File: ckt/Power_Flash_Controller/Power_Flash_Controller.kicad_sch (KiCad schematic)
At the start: 28 parts, among them J2 Screw_Terminal_01x03, J3 Screw_Terminal_01x03, J4 Screw_Terminal_01x03, K4 SANYOU_SRD_Form_C, K5 SANYOU_SRD_Form_C, K6 SANYOU_SRD_Form_C, Q1 BC857, Q2 BC857, Q3 BC857, U1 PC817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

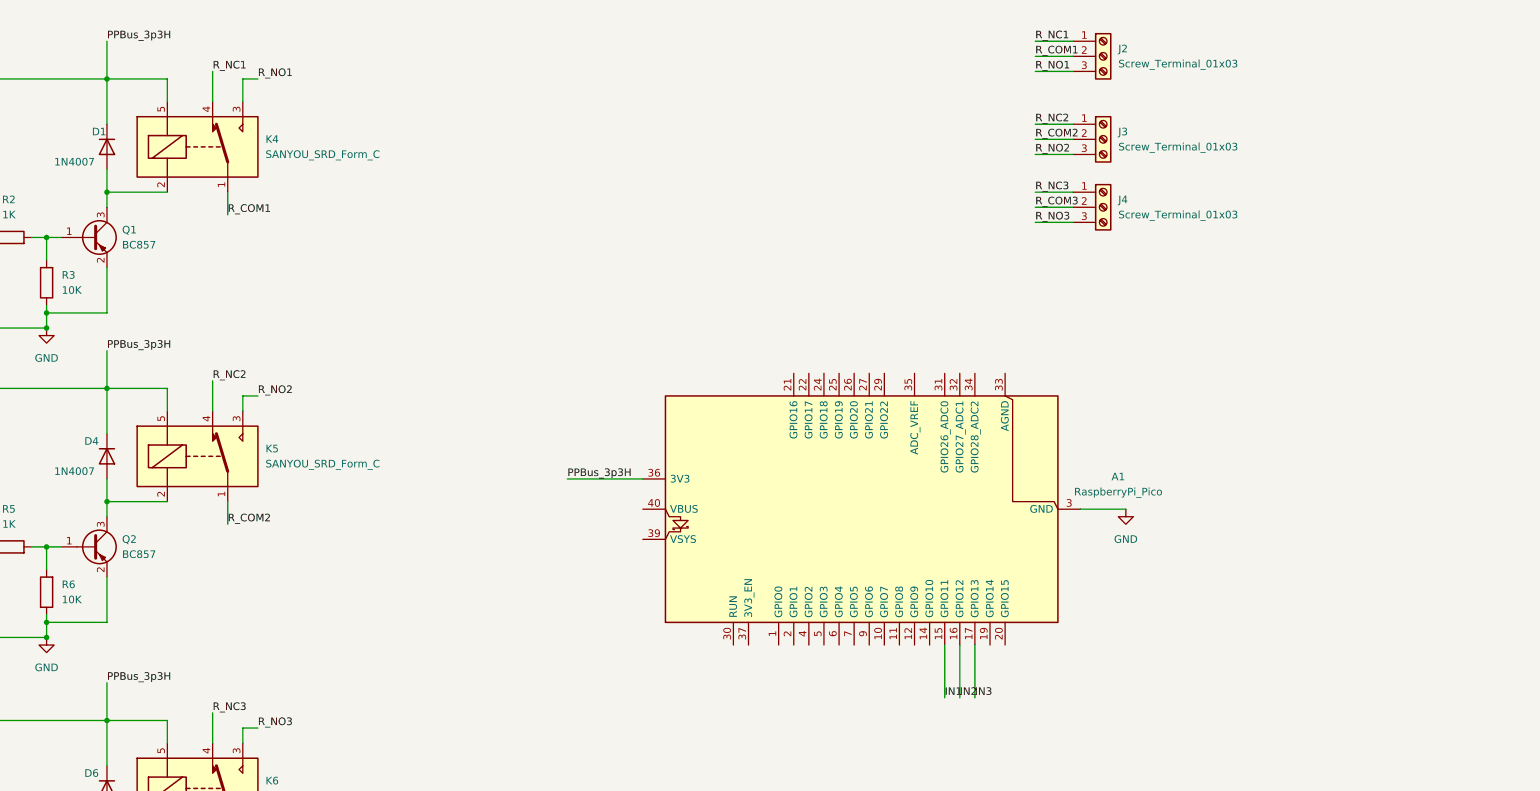
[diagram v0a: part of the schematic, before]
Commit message: Added connections for Ammeter and Voltmeter
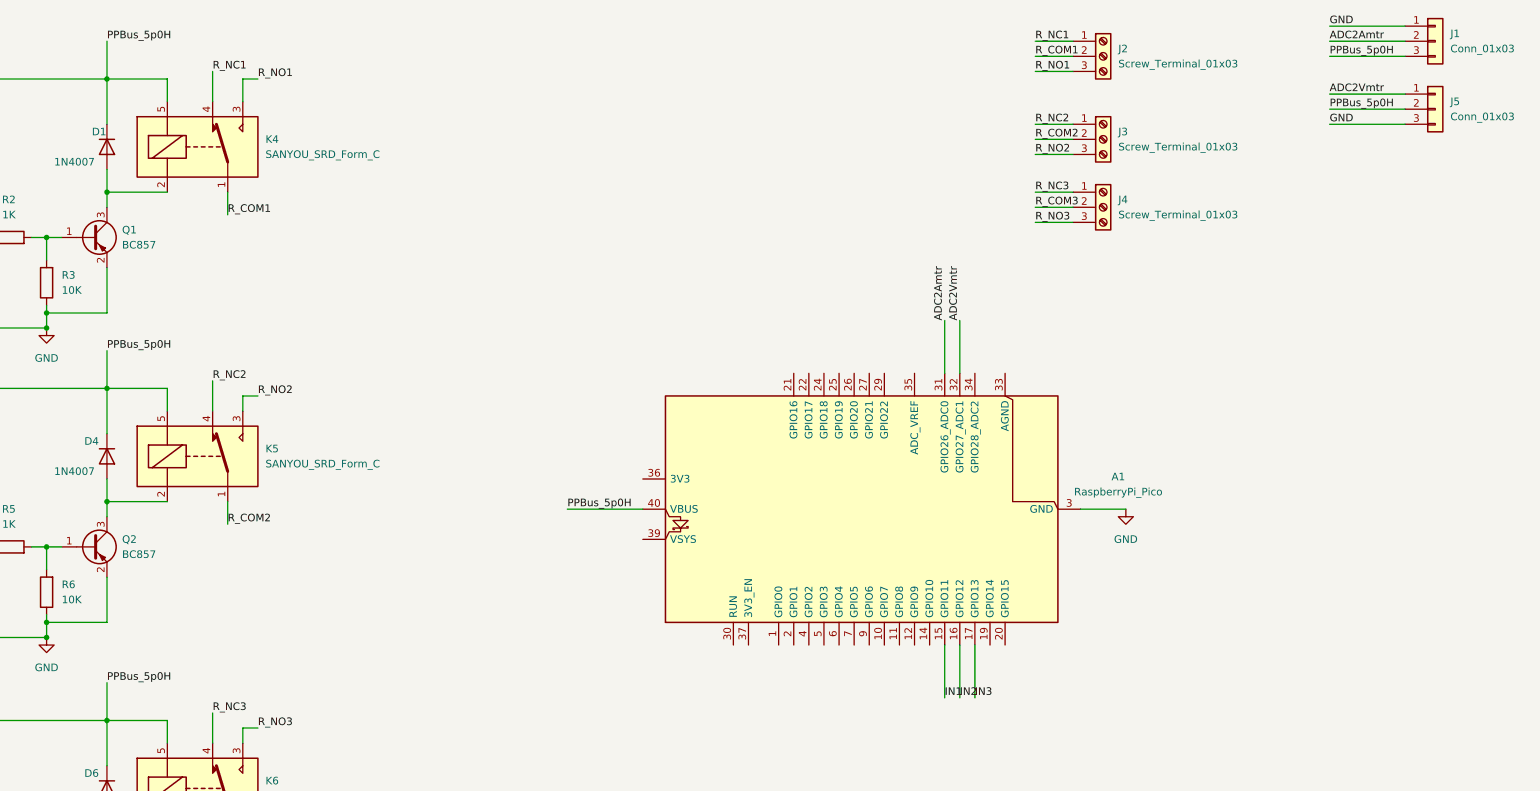
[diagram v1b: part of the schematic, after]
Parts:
- added J1, J5: Conn_01x03, Connector_PinHeader_2.54mm:PinHeader_1x03_P2.54mm_Vertical, symbol Connector_Generic:Conn_01x03
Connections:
- net GND: now also J1.1 (Pin_1), J5.3 (Pin_3)
- net ADC2Amtr: now reaches A1.31 (GPIO26_ADC0)
- net ADC2Amtr: now also J1.2 (Pin_2)
- net ADC2Vmtr: now reaches A1.32 (GPIO27_ADC1)
- net ADC2Vmtr: now also J5.1 (Pin_1)
- net PPBus_5p0H: now reaches A1.40 (VBUS)
- net PPBus_5p0H: now also D1.1 (K), D4.1 (K), D6.1 (K), K4.5, K5.5, K6.5, U1.4, U2.4, U3.4, J1.3 (Pin_3), J5.2 (Pin_2)
- removed net PPBus_3p3H: A1.36 (3V3), D1.1 (K), D4.1 (K), D6.1 (K), K4.5, K5.5, K6.5, U1.4, U2.4, U3.4

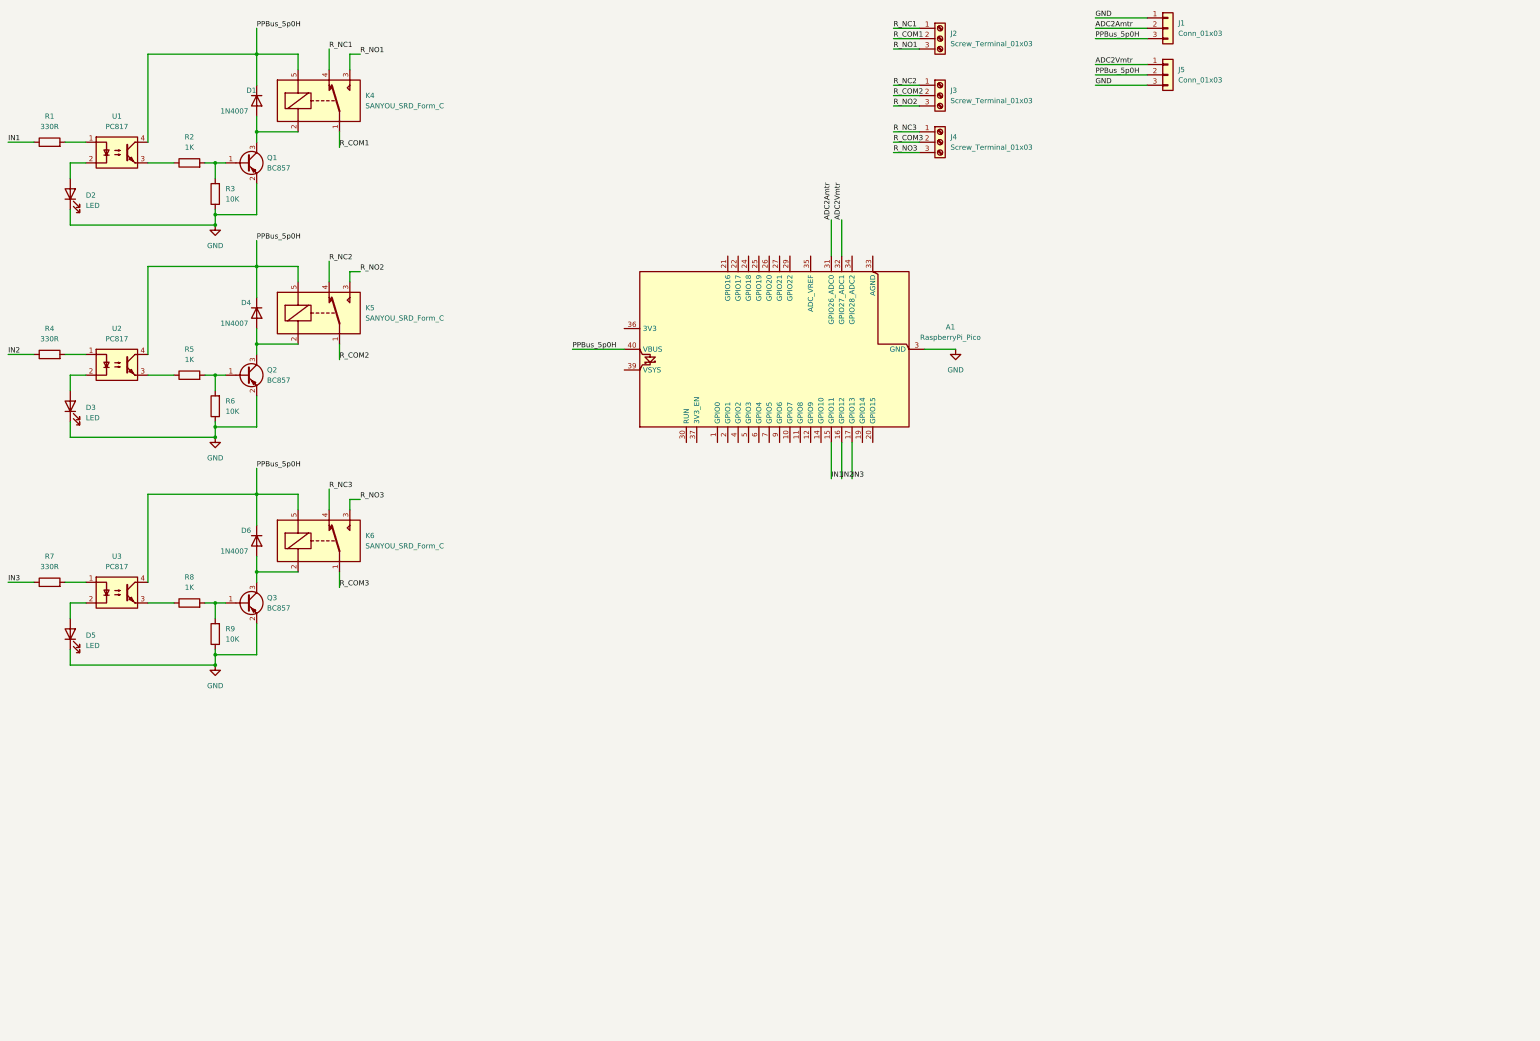
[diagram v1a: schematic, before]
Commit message: added relay no.4 and oled display mount, option for pwm fan and ammeter, voltmeter
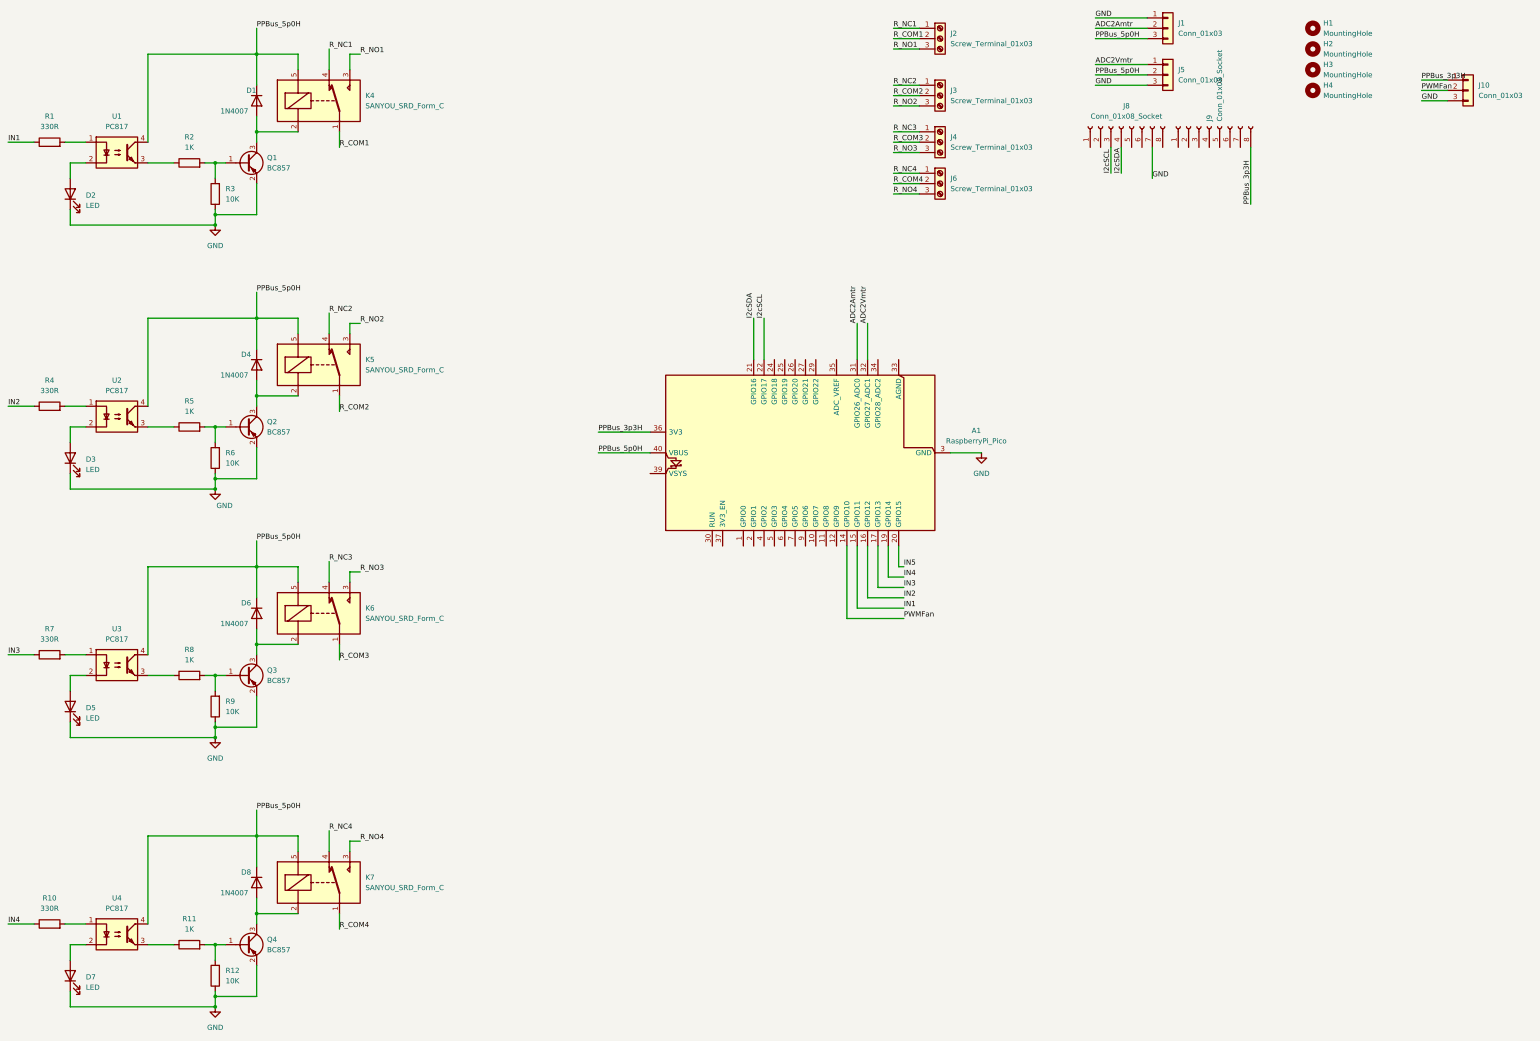
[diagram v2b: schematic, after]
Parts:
- added D7: LED, LED_THT:LED_D3.0mm_IRBlack, symbol Device:LED
- added D8: 1N4007, Diode_THT:D_DO-41_SOD81_P10.16mm_Horizontal, symbol Diode:1N4007
- added H1, H2, H3, H4: MountingHole, MountingHole:MountingHole_2.2mm_M2_DIN965_Pad_TopOnly, symbol Mechanical:MountingHole
- added J10: Conn_01x03, Connector_PinHeader_2.54mm:PinHeader_1x03_P2.54mm_Vertical, symbol Connector_Generic:Conn_01x03
- added J6: Screw_Terminal_01x03, TerminalBlock:TerminalBlock_MaiXu_MX126-5.0-03P_1x03_P5.00mm, symbol Connector:Screw_Terminal_01x03
- added J8, J9: Conn_01x08_Socket, Connector_PinHeader_2.54mm:PinHeader_1x08_P2.54mm_Vertical, symbol Connector:Conn_01x08_Socket
- added K7: SANYOU_SRD_Form_C, Relay_THT:Relay_SPDT_SANYOU_SRD_Series_Form_C, symbol Relay:SANYOU_SRD_Form_C
- added Q4: BC857, Package_TO_SOT_SMD:SOT-23, symbol Transistor_BJT:BC857
- added R10: 330R, Resistor_THT:R_Axial_DIN0204_L3.6mm_D1.6mm_P7.62mm_Horizontal, symbol Device:R
- added R11: 1K, Resistor_THT:R_Axial_DIN0204_L3.6mm_D1.6mm_P7.62mm_Horizontal, symbol Device:R
- added R12: 10K, Resistor_THT:R_Axial_DIN0204_L3.6mm_D1.6mm_P7.62mm_Horizontal, symbol Device:R
- added U4: PC817, Package_DIP:DIP-4_W7.62mm, symbol Isolator:PC817
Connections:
- net GND: now also D7.1 (K), J10.3 (Pin_3), J8.7 (Pin_7), Q4.2 (E), R12.1
- net PPBus_5p0H: now also D8.1 (K), K7.5, U4.4
- net PWMFan: now reaches A1.14 (GPIO10)
- net PWMFan: now also J10.2 (Pin_2)
- net IN4: now reaches A1.19 (GPIO14)
- net IN4: now also R10.1
- net IN5: now reaches A1.20 (GPIO15)
- net I2cSDA: now reaches A1.21 (GPIO16)
- net I2cSDA: now also J8.4 (Pin_4)
- net I2cSCL: now reaches A1.22 (GPIO17)
- net I2cSCL: now also J8.3 (Pin_3)
- net PPBus_3p3H: now reaches A1.36 (3V3)
- net PPBus_3p3H: now also J10.1 (Pin_1), J9.8 (Pin_8)
- new net: D8.2 (A), K7.2, Q4.3 (C)
- new net: R10.2, U4.1
- new net: D7.2 (A), U4.2
- new net: R11.1, U4.3
- new net: Q4.1 (B), R11.2, R12.2
- new net R_COM4: J6.2 (Pin_2), K7.1
- new net R_NC4: J6.1 (Pin_1), K7.4
- new net R_NO4: J6.3 (Pin_3), K7.3
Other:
- moved on the sheet: A1, D3, D4, D5, D6, K5, K6, Q2, Q3, R4, R5, R6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
